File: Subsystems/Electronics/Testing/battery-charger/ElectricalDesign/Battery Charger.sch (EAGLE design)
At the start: 0 parts

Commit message: General Battery Charger Schematic
Majority of components placed, absent items not in CIS components library. Many labels missing.
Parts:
- added BT1, BT2, BT3: Li-Ion, CougsInSpace-Energy:BATTERY-18650HG2
- added C1, C12, C13, C14, C2, C3: 1µF 10%, CougsInSpace-Capacitors:CAP-V-1UF-1608
- added C10, C11, C4, C9: 100nF 10%, CougsInSpace-Capacitors:CAP-V-100NF-1608
- added C15, C16, C17: 4.7µF 10%, CougsInSpace-Capacitors:CAP-V-4.7UF-3216
- added C5: 10µF 10%, CougsInSpace-Capacitors:CAP-V-10UF-1608
- added C6: 100nF 10%, CougsInSpace-Capacitors:CAP-H-100NF-1608
- added C7: 4.7pF ±0.1, CougsInSpace-Capacitors:CAP-V-4.7PF-1608
- added C8: 22pF 5%, CougsInSpace-Capacitors:CAP-V-22PF-1608
- added D1, D3, D4, D5: LTC4411, CougsInSpace-DiscreteSemi:LTC4411
- added D2: MBRM120LT, CougsInSpace-DiscreteSemi:DIODE-SCHOTTKY-H-POWERMITE
- added L1: 10µH 20%, CougsInSpace-Coils:INDUCTOR-H-10UH-6060
- added Q1, Q2: CSD16406Q3, CougsInSpace-DiscreteSemi:MOSFET-N-SON-3333
- added Q3, Q4, Q5: DMN2008LFU, CougsInSpace-DiscreteSemi:MOSFET_DUAL_COM_D-N-DMN2008LFU-UDFN-6-B
- added R1, R2: 10kΩ 0.1%, CougsInSpace-Resistors:RES-V-10K-1608
- added R10, R14, R6: 330Ω 1%, CougsInSpace-Resistors:RES-V-330R-1608
- added R11, R12, R15, R16, R7, R8: 4.75MΩ 1%, CougsInSpace-Resistors:RES-V-4.75M-1608
- added R13, R17, R9: 2.2kΩ 1%, CougsInSpace-Resistors:RES-V-2.2K-1608
- added R3: 10Ω 5%, CougsInSpace-Resistors:RES-V-10R-1608
- added R4: 47kΩ 0.1%, CougsInSpace-Resistors:RES-V-47K-1608
- added R5: 20kΩ 0.5%, CougsInSpace-Resistors:RES-V-20K-1608
- added U1: BQ24650, CougsInSpace-IC-Power:BQ24650
- added U2, U3, U4: BQ29700, CougsInSpace-IC-Power:BQ29700
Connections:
- new net 5.0V: D1.IN
- new net N$1: C2.1, U1.THERM_EN, U1.VREF
- new net N$10: Q1.G, U1.HIGHDV
- new net N$11: R4.1, R5.2, U1.MPPSET
- new net N$12: Q2.G, U1.LODRV
- new net N$13: R9.2, U2.V-
- new net N$14: R13.2, U3.V-
- new net N$15: C12.1, C13.1, C14.1, D3.IN, D4.IN, D5.IN
- new net N$16: Q3.G1, R8.2, U2.COUT
- new net N$17: Q3.G2, R7.2, U2.DOUT
- new net N$18: BT1.A, C9.2, Q3.S2, R7.1, U2.VSS
- new net N$19: Q4.G1, R12.2, U3.COUT
- new net N$2: C1.1, R3.1, U1.VCC
- new net N$20: C9.1, R6.1, U2.BAT
- new net N$21: BT1.C, C15.1, D3.OUT, R6.2
- new net N$22: Q4.G2, R11.2, U3.DOUT
- new net N$23: BT2.A, C10.2, Q4.S2, R11.1, U3.VSS
- new net N$24: C10.1, R10.1, U3.BAT
- new net N$25: BT2.C, C16.1, D4.OUT, R10.2
- new net N$26: R17.2, U4.V-
- new net N$27: Q5.G1, R16.2, U4.COUT
- new net N$28: Q5.G2, R15.2, U4.DOUT
- new net N$29: BT3.A, C11.2, Q5.S2, R15.1, U4.VSS
- new net N$3: C3.1, D2.A, U1.REGN
- new net N$30: C11.1, R14.1, U4.BAT
- new net N$31: BT3.C, C17.1, D5.OUT, R14.2
- new net N$4: C4.2, L1.1, Q1.S, Q2.D, U1.PH
- new net N$5: C4.1, D2.C, U1.BTST
- new net N$6: C5.1, D1.OUT, Q1.D, R3.2, R4.2
- new net N$7: C6.1, L1.2, U1.SR_P
- new net N$8: C6.2, C7.1, C8.1, R1.2, U1.SR_N
- new net N$9: C8.2, R1.1, R2.2, U1.VFB
- new net PGND: C1.2, C12.2, C13.2, C14.2, C15.2, C16.2, C17.2, C2.2, C3.2, C5.2, C7.2, D1.GND, D3.GND, D4.GND, D5.GND, Q2.S, Q3.S1, Q4.S1, Q5.S1, R12.1, R13.1, R16.1, R17.1, R2.1, R5.1, R8.1, R9.1, U1.PAD, U1.PGND
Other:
- note added: "Battery A 1 Cell With Protection IC"
- note added: "Battery B 1 Cell With Protection IC"
- note added: "Battery C 1 Cell With Protection IC"
- note added: "Battery Charger"
- note added: "Connector: To 5V 2A DC Adapter"
- note added: "Page 2"
- note added: "Page 3"
- note added: "Switching"

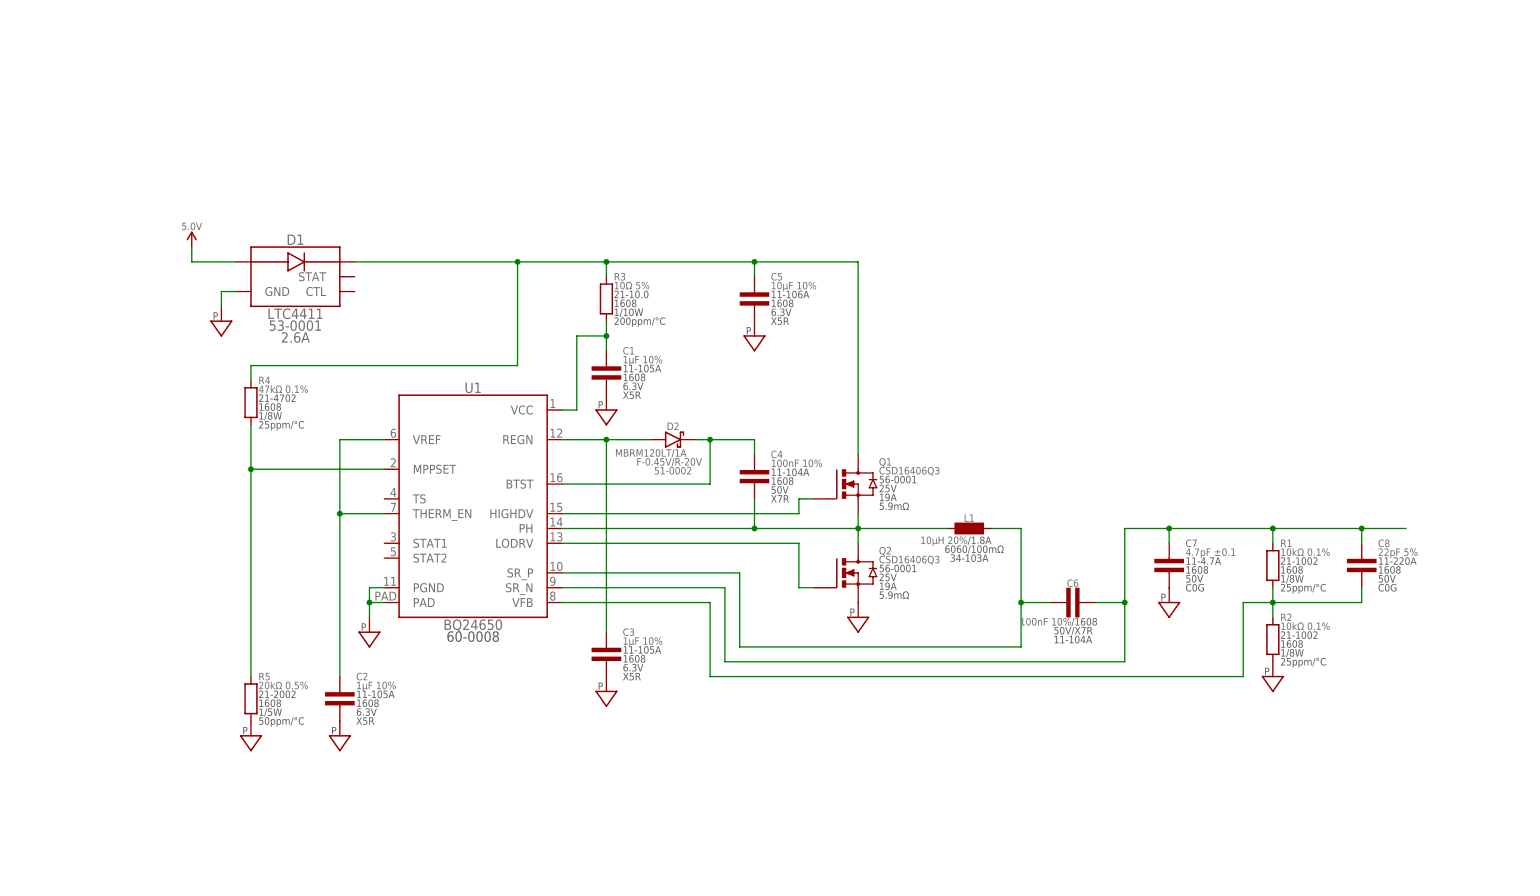
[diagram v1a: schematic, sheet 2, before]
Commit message: Partial changes
1/22/23
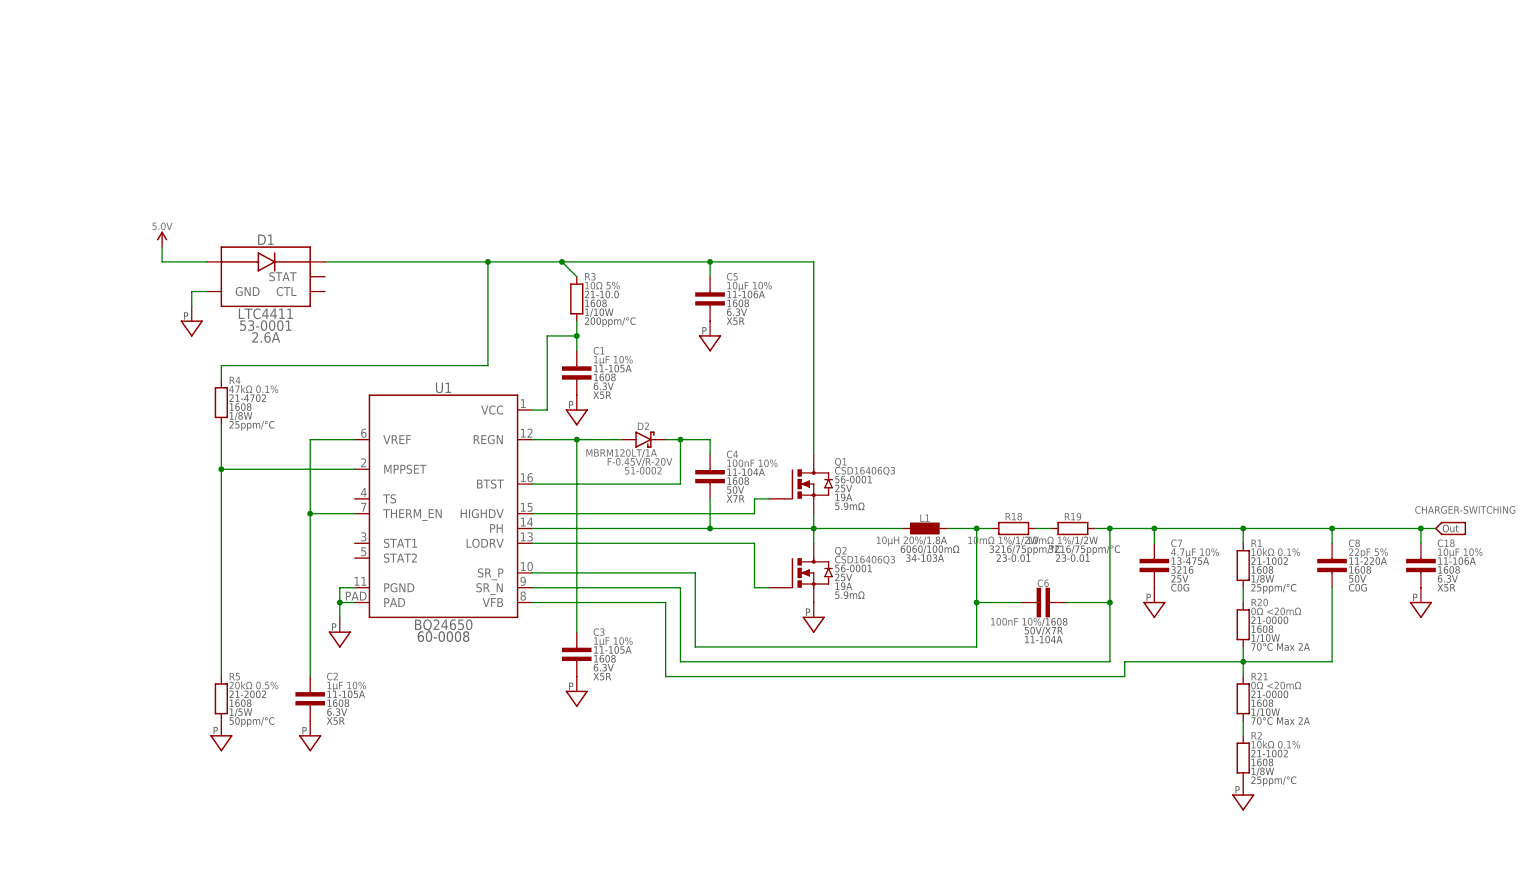
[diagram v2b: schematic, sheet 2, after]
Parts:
- added C18: 10µF 10%, CougsInSpace-Capacitors:CAP-V-10UF-1608
- added R18, R19: 10mΩ 1%, CougsInSpace-Resistors:RES-H-0.01R-3216
- added R20, R21: 0Ω <20mΩ, CougsInSpace-Resistors:RES-V-0-1608
- C7: value 4.7pF ±0.1 -> 4.7µF 10%; device CougsInSpace-Capacitors:CAP-V-4.7PF-1608 -> CougsInSpace-Capacitors:CAP-V-4.7UF-3216
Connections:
- new net CHARGER-SWITCHING: C12.1, C13.1, C14.1, C18.1, C6.2, C7.1, C8.1, D3.IN, D4.IN, D5.IN, R1.2, R19.2, U1.SR_N
- new net N$32: R2.2, R21.1
- net N$15: now also R1.1, R20.2; no longer C12.1, C13.1, C14.1, D3.IN, D4.IN, D5.IN
- net N$7: now also R18.1
- net N$8: now also R18.2, R19.1; no longer C6.2, C7.1, C8.1, R1.2, U1.SR_N
- net N$9: now also R20.1, R21.2; no longer R1.1, R2.2
- net PGND: now also C18.2
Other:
- moved on the sheet: C1, C2, C3, C4, C5, C6, C7, C8, D1, D2, L1, Q1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

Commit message: Added new blocks, still missing some components
No pages fully complete
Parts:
- added C19, C20: 1µF 10%, CougsInSpace-Capacitors:CAP-V-1UF-1608
- added J1: USB4515-GF-A_REVA, USB4515-GF-A_REVA:USB4515-GF-A_REVA
- added R22: CRGH2010J2R0, CRGH2010J2R0:CRGH2010J2R0
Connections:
- net 5.0V: now also J1.VBUS, R22.2
- net PGND: now also J1.GND, J1.SHIELD
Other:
- note added: "Lighting and Feedback"
- note added: "Page 4"
- note added: "Power Energizing Novel Integrated System (PENIS)"

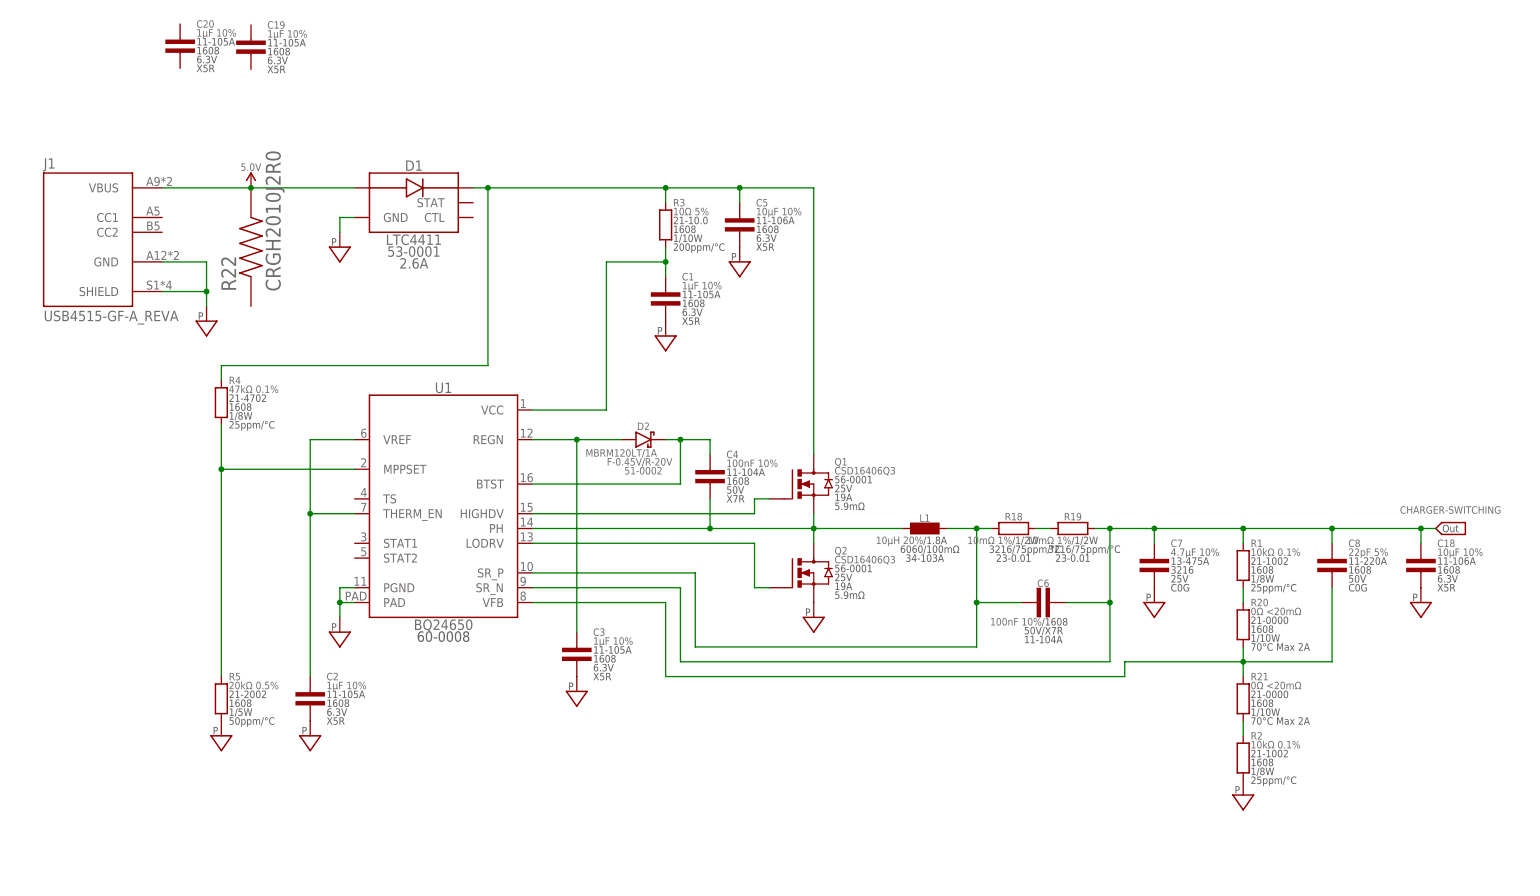
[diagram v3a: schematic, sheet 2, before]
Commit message: Finished Switching and Battery Protection Circuits
Pages 1-3 are basically finished, while the main components for page 4 have been imported
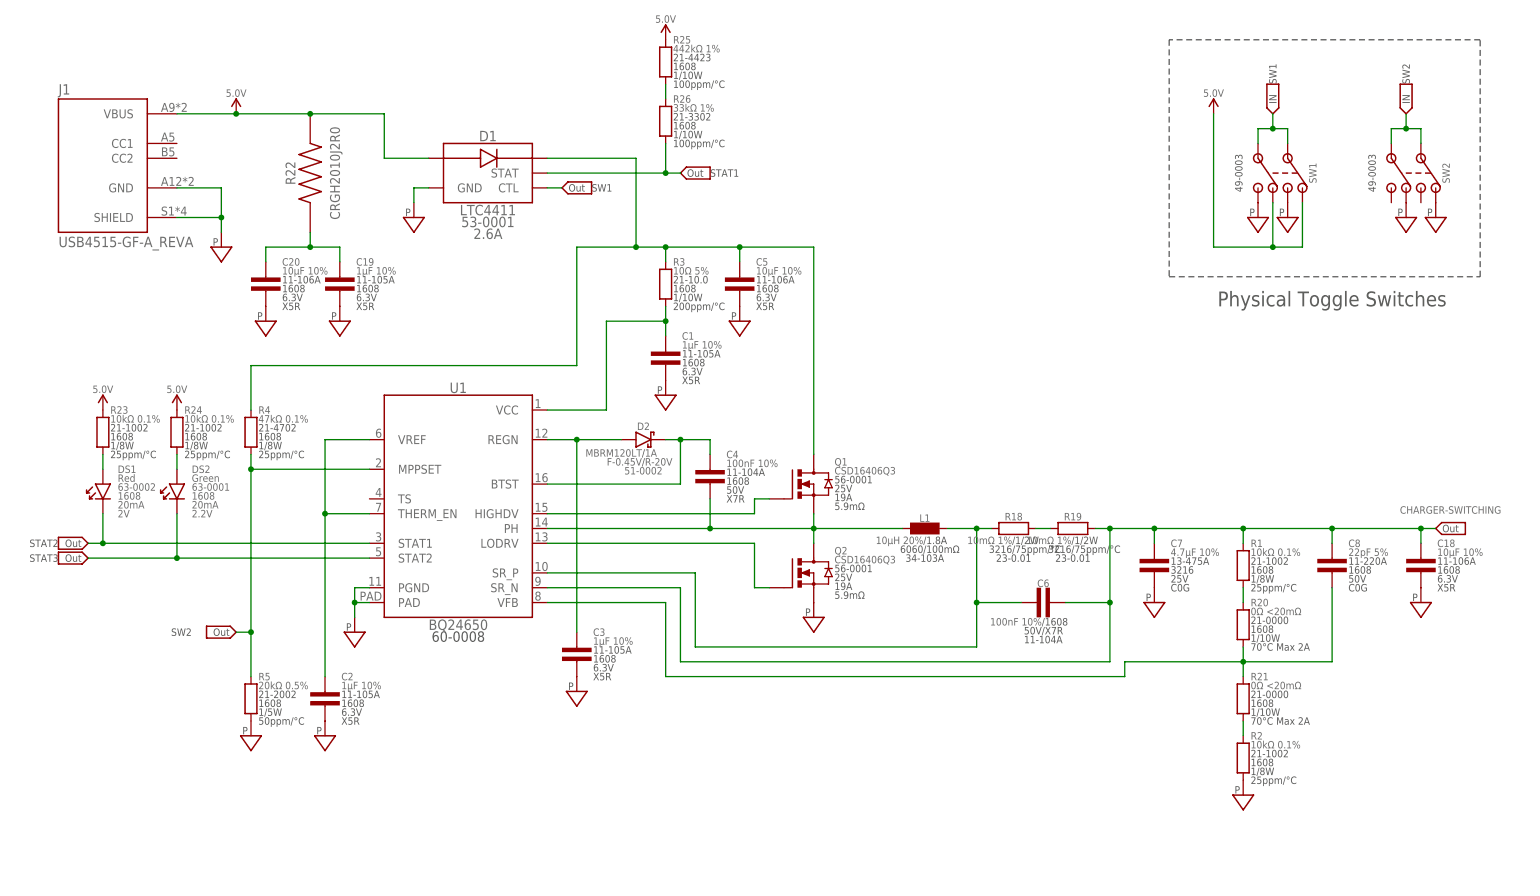
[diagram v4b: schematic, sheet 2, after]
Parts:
- added DS1: Red, CougsInSpace-LEDs:LED-V-RED-1608
- added DS2: Green, CougsInSpace-LEDs:LED-V-GRN-1608
- added R23, R24: 10kΩ 0.1%, CougsInSpace-Resistors:RES-V-10K-1608
- added R25, R28, R30, R32: 442kΩ 1%, CougsInSpace-Resistors:RES-V-442K-1608
- added R26, R27, R29, R31: 33kΩ 1%, CougsInSpace-Resistors:RES-V-33K-1608
- added SW1, SW2, SW3, SW4, SW5: (no value), CougsInSpace-Switches:SWITCH-DPDT-100DP1T1B1M2QE
- added U5: ESP32-S2-MINI-1, ESP32-S2-MINI-1:ESP32-S2-MINI-1
- added U7: LT1129IS8-3.3, LT1129IS8-3.3:LT1129IS8-3.3
- C20: value 1µF 10% -> 10µF 10%; device CougsInSpace-Capacitors:CAP-V-1UF-1608 -> CougsInSpace-Capacitors:CAP-V-10UF-1608
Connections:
- new net N$21: U7.OUTPUT, U7.SENSE/ADJ
- new net N$33: DS2.A, R24.1
- new net N$34: C19.1, C20.1, R22.1
- new net N$35: R25.1, R26.2
- new net N$36: R27.2, R28.1
- new net N$37: R29.2, R30.1
- new net N$38: R31.2, R32.1
- new net STAT1: D1.STAT, R26.1
- new net STAT2: DS1.C, U1.STAT1
- new net STAT3: DS2.C, U1.STAT2
- new net STAT4: D3.STAT, R27.1
- new net STAT5: D4.STAT, R29.1
- new net STAT6: D5.STAT, R31.1
- new net SW1: D1.CTL, SW1.COM-A, SW1.COM-B
- new net SW2: R4.1, R5.2, SW2.COM-A, SW2.COM-B, U1.MPPSET
- new net SW3: D3.CTL, SW3.COM-A, SW3.COM-B
- new net SW4: D4.CTL, SW4.COM-A, SW4.COM-B
- new net SW5: D5.CTL, SW5.COM-A, SW5.COM-B
- net 5.0V: now also R23.2, R24.2, R25.2, R28.2, R30.2, R32.2, SW1.1-A, SW1.1-B, SW3.1-A, SW3.1-B, SW4.1-A, SW4.1-B, SW5.1-A, SW5.1-B, U7.VIN
- net N$11: now also DS1.A, R23.1; no longer R4.1, R5.2, U1.MPPSET
- net PGND: now also C19.2, C20.2, SW1.2-A, SW1.2-B, SW2.1-A, SW2.1-B, SW3.2-A, SW3.2-B, SW4.2-A, SW4.2-B, SW5.2-A, SW5.2-B, U7.GND, U7.GND_2, U7.GND_3
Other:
- note added: "Lighting and Display"
- note added: "Performance and Error Notification Integrated Circuit (PENIC)"
- note added: "Physical Toggle Switches"
- note added: "STAT1"
- note added: "STAT2"
- note added: "STAT3"
- note added: "STAT4"
- note added: "STAT5"
- note added: "STAT6"
- note added: "SW1"
- note added: "SW2"
- note added: "SW3"
- note added: "SW4"
- note added: "SW5"
- note removed: "Lighting and Feedback"
- note removed: "Power Energizing Novel Integrated System (PENIS)"
- moved on the sheet: C1, C12, C13, C14, C15, C16, C17, C19, C2, C20, C5, D1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

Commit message: USB to UART IC Added
Page 4 should now be complete with the implementation of a USB to UART program converter. ESP32 has been moved to page 5 and outside of the thermistor connection on the charge controller, this should be the last page
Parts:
- added C25, C26: 4.7µF 10%, CougsInSpace-Capacitors:CAP-V-4.7UF-3216
- added C27, C28, C30, C31: 100nF 10%, CougsInSpace-Capacitors:CAP-V-100NF-1608
- added C29: 10µF 10%, CougsInSpace-Capacitors:CAP-V-10UF-1608
- added C32: C1206C226K8RACTU, C1206C226K8RACTU:C1206C226K8RACTU
- added DS3, DS4: Green, CougsInSpace-LEDs:LED-V-GRN-1608
- added J2: (no value), CougsInSpace-Connectors:USB-B-FEMALE
- added Q6, Q7: BC817, BC817:BC817
- added R33, R34: 10kΩ 0.1%, CougsInSpace-Resistors:RES-H-10K-1608
- added R35, R36: 10kΩ 0.1%, CougsInSpace-Resistors:RES-V-10K-1608
- added U$1: LD1117AS33, LD1117AS33:LD1117AS33
- U5: value ESP32-S2-MINI-1 -> CP2102N-A02-GQFN28; device ESP32-S2-MINI-1:ESP32-S2-MINI-1 -> CP2102N-A02-GQFN28:CP2102N-A02-GQFN28
- U7: value LT1129IS8-3.3 -> ESP32-S2-MINI-1; device LT1129IS8-3.3:LT1129IS8-3.3 -> ESP32-S2-MINI-1:ESP32-S2-MINI-1
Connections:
- new net N$25: J2.DATA_P, U5.D+
- new net N$31: J2.DATA_N, U5.D-
- new net N$42: C25.1, C27.1, J2.VCC, R35.2, R36.2, U5.VBUS, U5.VREGIN
- new net N$43: DS4.C, U5.GPIO.1/RXT
- new net N$44: C29.1, C31.1, C32.2, U$1.V_OUT, U7.3V3
- new net N$45: DS3.C, U5.GPIO.0/TXT
- new net N$46: Q6.E, R34.1, U5.RTS
- new net N$47: Q7.E, R33.1, U5.DTR
- new net N$48: Q7.B, R34.2
- new net N$49: Q6.B, R33.2
- new net N$50: DS3.A, R35.1
- new net N$51: DS4.A, R36.1
- new net UART-ESP_EN: Q6.C
- new net UART-ESP_IO0: Q7.C
- new net UART_RXD-ESP_TXD: U5.RXD
- new net UART_TXD-ESP_RXD: U5.TXD
- net 5.0V: now also C30.1, U$1.V_IN; no longer U7.VIN
- net N$21: now also C26.1, C28.1, U5.VDD; no longer U7.OUTPUT, U7.SENSE/ADJ
- net PGND: now also C25.2, C26.2, C27.2, C28.2, C29.2, C30.2, C31.2, C32.1, J2.GND, J2.SHIELD, U$1.GND, U5.GND; no longer U7.GND_2, U7.GND_3
- net STAT1: now also U7.IO1
- net STAT2: now also U7.IO2
- net STAT3: now also U7.IO3
- net STAT4: now also U7.IO4
- net STAT5: now also U7.IO5
- net STAT6: now also U7.IO6
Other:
- note added: "22uF 10%"
- note added: "5V to 3.3V Linear Regulator"
- note added: "Change"
- note added: "Connector: 5V 3A DC Adapter"
- note added: "Connector: USB Data In"
- note added: "Design Note: For the UART to properly communicate with the ESP the EN pin must have >= 100nF cap to ground and >= 10k pullup"
- note added: "Page 5"
- note added: "Performance and Error Notification IC (PENIC) With Power Regulation"
- note added: "USB to UART Programming Converter"
- note removed: "Connector: To 5V 2A DC Adapter"
- note removed: "Performance and Error Notification Integrated Circuit (PENIC)"
